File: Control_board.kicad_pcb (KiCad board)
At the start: 2 copper layers, 192 x 122 mm, 48 parts, among them IC1 HCPL2731M, IC2 HCPL2731M, IC3 CNY74-2H, IC4 CNY74-2H, K1 SR11-3V-200-2C, K2 SR5-12V-200-1C, K3 SR5-3V-200-1C, K4 SR5-3V-200-1C, K5 SR11-3V-200-2C, U1 Teensy4.1

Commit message: V1.2 Updates
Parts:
- added D1: 1N4001, Diode_THT:D_DO-41_SOD81_P10.16mm_Horizontal, F.Cu at (163.0, 65.0)
- added D2: 1N4001, Diode_THT:D_DO-41_SOD81_P10.16mm_Horizontal, F.Cu at (156.0, 75.0)
- IC1, IC2: value HCPL2731M -> CNY74-2H
- R1, R10, R11, R12, R13, R14, R15, R16, R17, R18, R19, R20, R3, R4, R5, R6, R7, R8, R9: footprint Resistor_THT:R_Axial_DIN0411_L9.9mm_D3.6mm_P12.70mm_Horizontal -> SamacSys:R_Axial_DIN0411_L9.9mm_D3.6mm_P12.70mm_Horizontal_ZT
- R2: value 6.19K -> 6.8K; footprint Resistor_THT:R_Axial_DIN0411_L9.9mm_D3.6mm_P12.70mm_Horizontal -> SamacSys:R_Axial_DIN0411_L9.9mm_D3.6mm_P12.70mm_Horizontal_ZT
- moved R18 136.0 mm to (57.0, 44.7)
- moved R16 128.9 mm to (55.0, 113.7)
- moved R15 126.6 mm to (50.0, 113.7)
- moved R20 118.4 mm to (52.0, 44.7)
- moved R14 109.6 mm to (55.0, 96.7)
- moved R13 107.2 mm to (50.0, 96.7)
- moved R5 92.4 mm to (42.7, 57.0)
- moved R6 91.5 mm to (30.0, 52.0)
- moved R19 88.5 mm to (59.7, 57.0)
- moved R17 88.0 mm to (59.7, 52.0)
- moved R3 82.1 mm to (46.0, 32.3)
- moved R1 79.7 mm to (41.0, 32.3)
- moved R4 77.2 mm to (36.0, 45.0)
- moved K3 76.7 mm to (100.5, 69.2), turned to 0 degrees
- moved R2 74.7 mm to (31.0, 45.0)
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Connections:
- IC1 pad 5: 3.3V -> Net-(IC1-E_1)
- IC1 pad 6: Net-(IC1-C_3) -> 3.3V
- IC1 pad 7: Net-(IC1-C_4) -> 3.3V
- IC1 pad 8: 3.3V -> Net-(IC1-E_2)
- IC2 pad 5: 5VDC -> Net-(IC2-E_1)
- IC2 pad 6: Net-(IC2-C_3) -> 5VDC
- IC2 pad 7: Net-(IC2-C_4) -> 5VDC
- IC2 pad 8: 5VDC -> Net-(IC2-E_2)
- IC3 pad 5: 3.3V -> Net-(IC3-E_1)
- IC3 pad 6: P3I -> 3.3V
- IC3 pad 7: Net-(IC3-C_4) -> 5VDC
- IC3 pad 8: 5VDC -> P3I
- IC4 pad 5: 3.3V -> Net-(IC4-E_1)
- IC4 pad 6: P4I -> 3.3V
- IC4 pad 7: Net-(IC4-C_4) -> 5VDC
- IC4 pad 8: 5VDC -> P4I
- K1 pad 4: Net-(IC2-C_4) -> Net-(IC2-E_2)
- K1 pad 5: Net-(IC2-C_3) -> Net-(IC2-E_1)
- K2 pad 5: 12COM -> 12COM_C
- K5 pad 4: Net-(IC3-C_4) -> Net-(IC3-E_1)
- K5 pad 5: Net-(IC4-C_4) -> Net-(IC4-E_1)
- LED1 pad 1: 12COM -> 12COM_C
- PS1 pad 1: 12VDC -> 12VDC_C
- PS1 pad 2: 12COM -> 12COM_C
- R10 pad 2: Net-(IC1-C_4) -> Net-(IC1-E_2)
- R14 pad 2: Net-(IC4-C_4) -> Net-(IC4-E_1)
- R15 pad 2: Net-(IC3-C_4) -> Net-(IC3-E_1)
- R2 pad 1: 12VDC -> 12VDC_C
- R7 pad 2: Net-(IC2-C_4) -> Net-(IC2-E_2)
- R8 pad 2: Net-(IC2-C_3) -> Net-(IC2-E_1)
- R9 pad 2: Net-(IC1-C_3) -> Net-(IC1-E_1)
- U1 pad 13: Net-(IC1-C_4) -> Net-(IC1-E_2)
- U1 pad 14: Net-(IC1-C_3) -> Net-(IC1-E_1)
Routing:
- net 12VDC_C: track 0.00 -> 152.3 mm
- net 12COM_C: track 0.00 -> 142.1 mm, vias 0 -> 1
- net Net-(A4C1-Pin_2): track 27.7 -> 169.2 mm, vias 0 -> 1
- net Net-(IC3-A_2): track 9.93 -> 140.2 mm
- net Net-(IC1-E_2): track 0.00 -> 127.8 mm
- net Net-(A3C1-Pin_2): track 26.4 -> 152.4 mm, vias 0 -> 2
- net 12COM: track 136.1 -> 14.3 mm
- net Net-(IC2-E_1): track 0.00 -> 117.9 mm
- net Net-(IC3-E_1): track 0.00 -> 113.6 mm, vias 0 -> 1
- net Net-(IC4-A_2): track 18.5 -> 127.8 mm, vias 0 -> 1
- net Net-(IC2-A_2): track 4.83 -> 111.6 mm, vias 0 -> 1
- net Net-(IC1-E_1): track 0.00 -> 104.8 mm
- net Net-(IC1-A_2): track 7.38 -> 111.9 mm
- net Net-(IC1-A_1): track 7.43 -> 110.5 mm, vias 0 -> 1
- net Net-(IC2-A_1): track 5.02 -> 104.3 mm
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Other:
- board size 192 x 122 mm -> 163 x 122 mm
- board text added: "12V"
- board text added: "5V"
- board text added: "AUTO"
- board text added: "FLT"

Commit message: Version 1.2
Mouser Project: https://www.mouser.com/ProjectManager/ProjectDetail.aspx?AccessID=017e74ae19
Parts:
- added 12VOut1: Conn_01x02_Pin, Connector_Phoenix_MC_HighVoltage:PhoenixContact_MCV_1,5_2-G-5.08_1x02_P5.08mm_Vertical, F.Cu at (146.3, 54.5)
- added 5VOut1: Conn_01x02_Pin, Connector_Phoenix_MC_HighVoltage:PhoenixContact_MCV_1,5_2-G-5.08_1x02_P5.08mm_Vertical, F.Cu at (146.3, 66.5)
- added J1: Conn_01x02_Pin, Connector_PinHeader_2.54mm:PinHeader_1x02_P2.54mm_Vertical, F.Cu at (113.0, 116.5)
- added U2: 01530007Z, SamacSys:01530007Z, F.Cu at (173.7, 60.2)
- added U3: 01530007Z, SamacSys:01530007Z, F.Cu at (173.7, 80.8)
- moved D1 18.5 mm to (151.0, 79.1)
- moved D2 18.5 mm to (144.0, 89.1)
- moved A3C1 8.54 mm to (147.0, 114.0)
- moved A3M1 8.54 mm to (151.0, 114.0)
- moved A4C1 8.54 mm to (155.0, 114.0)
- moved A4M1 8.54 mm to (159.0, 114.0)
- moved IL1 8.54 mm to (131.0, 114.0)
- moved IR1 8.54 mm to (139.0, 114.0)
- moved ML1 8.54 mm to (135.0, 114.0)
- moved MR1 8.54 mm to (143.0, 114.0)
- moved PWR_InF1 7.45 mm to (158.4, 95.3)
- moved R1 3.50 mm to (40.0, 35.6)
- moved R17 3.50 mm to (58.7, 55.4)
- moved R19 3.50 mm to (58.7, 60.4)
- moved R2 3.50 mm to (30.0, 48.4)
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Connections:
- D1 pad 1: 12VDC_C -> 12VDC_A
- IC3 pad 5: Net-(IC3-E_1) -> A3C_IN
- IC3 pad 8: P3I -> Net-(IC3-E_1)
- IC4 pad 5: Net-(IC4-E_1) -> A4C_IN
- IC4 pad 8: P4I -> Net-(IC4-E_1)
- K3 pad 1: unconnected-(K3-NC-Pad1) -> Net-(EKill1-Pin_1)
- K3 pad 6: Net-(EKill1-Pin_1) -> unconnected-(K3-NO-Pad6)
- PS1 pad 3: 5VDC -> 5VDC_A
- R13 pad 2: P3I -> A3C_IN
- R16 pad 2: P4I -> A4C_IN
- R17 pad 2: P4O -> A4M_OUT
- R19 pad 2: P3O -> A3M_OUT
- U1 pad 15: 3.3V -> unconnected-(U1-3V3-Pad15)
- U1 pad 28: P4O -> A4C_IN
- U1 pad 29: P4I -> A4M_OUT
- U1 pad 44: P3O -> A3C_IN
- U1 pad 45: P3I -> A3M_OUT
- U1 pad 46: unconnected-(U1-3V3-Pad46) -> 3.3V
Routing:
- net A4C_IN: track 0.00 -> 125.1 mm, vias 0 -> 2
- net P4I: track 118.7 -> 0.00 mm, vias 1 -> 0
- net P3I: track 111.2 -> 0.00 mm, vias 2 -> 0
- net A3C_IN: track 0.00 -> 105.7 mm, vias 0 -> 1
- net 5VDC_A: track 0.00 -> 60.9 mm
- net P3O: track 56.6 -> 0.00 mm, vias 1 -> 0
- net A3M_OUT: track 0.00 -> 51.6 mm, vias 0 -> 2
- net Net-(IR1-Pin_2): track 136.4 -> 177.3 mm
- net 3.3V: track 84.6 -> 120.0 mm, vias 0 -> 1
- net MOut: track 137.6 -> 104.3 mm, vias 0 -> 1
- net 5VDC: track 301.7 -> 268.6 mm
- net A4M_OUT: track 0.00 -> 30.8 mm
- net Net-(A4C1-Pin_2): track 169.2 -> 199.7 mm
- net 12COM_C: track 142.1 -> 172.6 mm, vias 1 -> 0
- net P4O: track 28.8 -> 0.00 mm
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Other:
- outline, holes or cut-outs redrawn
- board text added: "12Com Out"
- board text added: "12V Fuse 1A"
- board text added: "12VDC"
- board text added: "5V Fuse 3A"
- board text added: "5V Jumper Board to Motor"
- board text added: "5VCom Out"
- board text added: "5VDC Out"

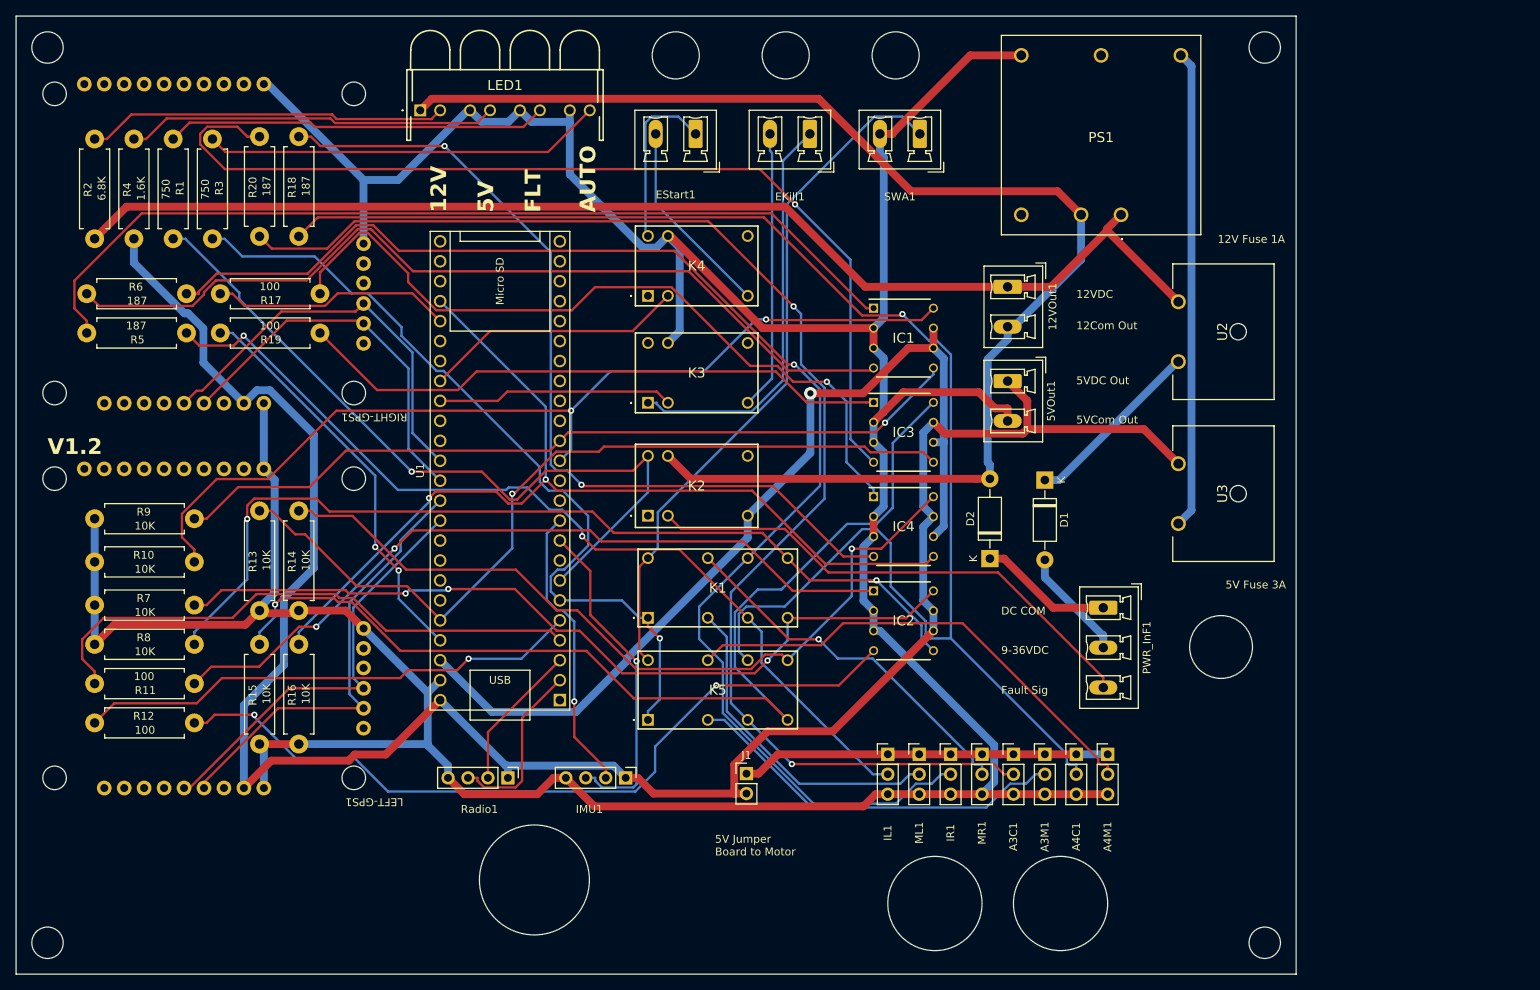
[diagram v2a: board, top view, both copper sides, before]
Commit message: Swapped Signal and 5+
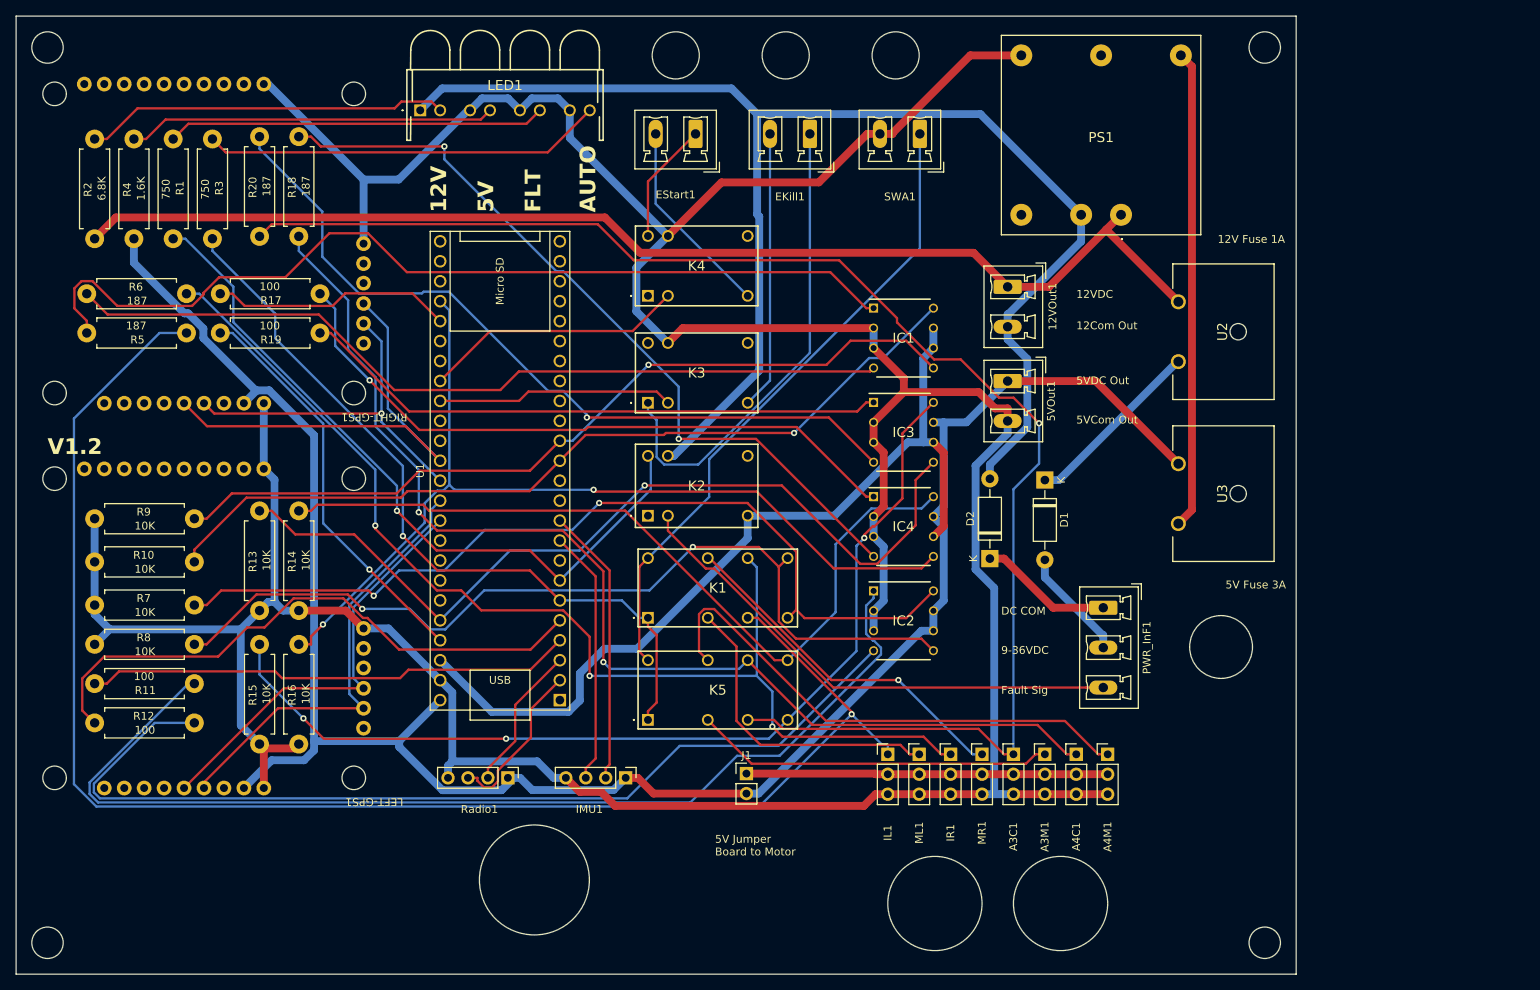
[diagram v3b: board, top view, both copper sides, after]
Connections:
- A3C1 pad 1: M5V -> Net-(A3C1-Pin_1)
- A3C1 pad 2: Net-(A3C1-Pin_2) -> M5V
- A3M1 pad 1: M5V -> Net-(A3M1-Pin_1)
- A3M1 pad 2: Net-(A3M1-Pin_2) -> M5V
- A4C1 pad 1: M5V -> Net-(A4C1-Pin_1)
- A4C1 pad 2: Net-(A4C1-Pin_2) -> M5V
- A4M1 pad 1: M5V -> Net-(A4M1-Pin_1)
- A4M1 pad 2: Net-(A4M1-Pin_2) -> M5V
- IL1 pad 1: M5V -> Net-(IL1-Pin_1)
- IL1 pad 2: Net-(IL1-Pin_2) -> M5V
- IR1 pad 1: M5V -> Net-(IR1-Pin_1)
- IR1 pad 2: Net-(IR1-Pin_2) -> M5V
- K1 pad 3: Net-(IL1-Pin_2) -> Net-(IL1-Pin_1)
- K1 pad 6: Net-(IR1-Pin_2) -> Net-(IR1-Pin_1)
- K5 pad 2: Net-(A3M1-Pin_2) -> Net-(A3M1-Pin_1)
- K5 pad 3: Net-(A3C1-Pin_2) -> Net-(A3C1-Pin_1)
- K5 pad 6: Net-(A4C1-Pin_2) -> Net-(A4C1-Pin_1)
- K5 pad 7: Net-(A4M1-Pin_2) -> Net-(A4M1-Pin_1)
- ML1 pad 1: M5V -> Net-(K1-COM_1)
- ML1 pad 2: Net-(K1-COM_1) -> M5V
- MR1 pad 1: M5V -> Net-(K1-COM_2)
- MR1 pad 2: Net-(K1-COM_2) -> M5V
- R18 pad 1: Net-(A4C1-Pin_2) -> Net-(A4C1-Pin_1)
- R20 pad 1: Net-(A3C1-Pin_2) -> Net-(A3C1-Pin_1)
- R5 pad 1: Net-(IL1-Pin_2) -> Net-(IL1-Pin_1)
- R6 pad 2: Net-(IR1-Pin_2) -> Net-(IR1-Pin_1)
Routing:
- net Net-(A4C1-Pin_2): track 199.7 -> 0.00 mm, vias 1 -> 0
- net Net-(IL1-Pin_1): track 0.00 -> 196.4 mm, vias 0 -> 1
- net Net-(A3C1-Pin_1): track 0.00 -> 189.9 mm, vias 0 -> 1
- net Net-(IR1-Pin_2): track 177.3 -> 0.00 mm, vias 1 -> 0
- net Net-(A3C1-Pin_2): track 171.4 -> 0.00 mm, vias 2 -> 0
- net Net-(IR1-Pin_1): track 0.00 -> 147.0 mm, vias 0 -> 3
- net Net-(A4C1-Pin_1): track 0.00 -> 145.6 mm, vias 0 -> 2
- net Net-(IL1-Pin_2): track 116.7 -> 0.00 mm, vias 2 -> 0
- net Net-(A4M1-Pin_1): track 0.00 -> 66.3 mm
- net Net-(A4M1-Pin_2): track 61.8 -> 0.00 mm
- net Net-(A3M1-Pin_2): track 49.3 -> 0.00 mm
- net Net-(A3M1-Pin_1): track 0.00 -> 45.7 mm
- net Net-(IC2-A_1): track 97.8 -> 138.4 mm, vias 2 -> 0
- net Net-(IC3-A_2): track 125.7 -> 100.0 mm
- net Net-(IC2-A_2): track 100.4 -> 124.5 mm, vias 2 -> 0
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
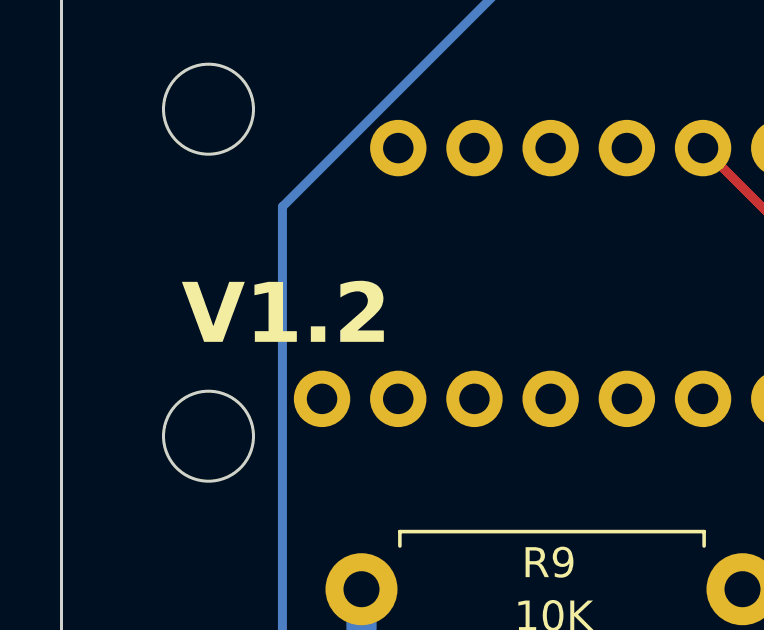
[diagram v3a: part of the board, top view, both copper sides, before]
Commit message: Updated revision number to 1.3
This version swapped the +5V and Signal to the motors and from the  controller to match the RC standard https://learn.sparkfun.com/tutorials/hobby-servo-tutorial/all where the center is +5V and the pin 3 is the control signal.
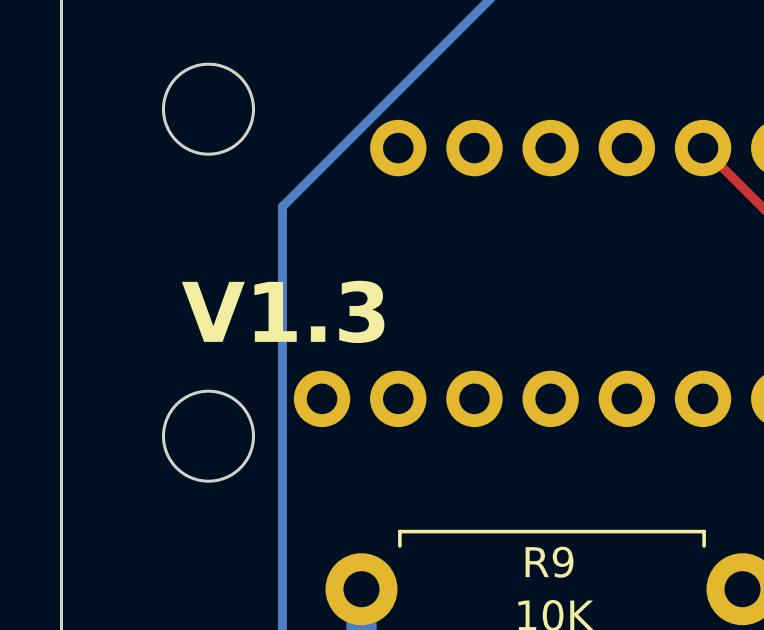
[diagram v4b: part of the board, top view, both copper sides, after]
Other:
- board text added: "${REVISION}"
- board text removed: "V1.2"
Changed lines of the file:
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@@
     (title "AGV Control Board")
     (date "2024-06-30")
-    (rev "V1.0")
+    (rev "V1.3")
   )
   (layers
@@
     (effects (font (size 2 2) (thickness 0.4) bold) (justify left bottom))
   )
-  (gr_text "V1.2" (at 24 76) (layer "F.SilkS")
+  (gr_text "${REVISION}" (at 24 76) (layer "F.SilkS")
     (effects (font (size 2 2) (thickness 0.4) bold) (justify left bottom))
   )
